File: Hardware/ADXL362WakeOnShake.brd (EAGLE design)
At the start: 43.2 x 24.1 mm, 24 parts, among them J1 PROG_HDR, U1 ADXL362, U3 ADP160-3.3

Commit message: Added attribution for original concept.
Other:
- board text added: "Original wake-on-shake concept by Nitzan Gadish, Analog Devices"
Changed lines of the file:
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@@
 <layers>
 <layer number="1" name="Top" color="4" fill="1" visible="yes" active="yes"/>
-<layer number="2" name="Route2" color="1" fill="3" visible="no" active="yes"/>
-<layer number="15" name="Route15" color="4" fill="6" visible="no" active="yes"/>
+<layer number="2" name="Route2" color="1" fill="3" visible="yes" active="yes"/>
+<layer number="15" name="Route15" color="4" fill="6" visible="yes" active="yes"/>
 <layer number="16" name="Bottom" color="1" fill="1" visible="yes" active="yes"/>
 <layer number="17" name="Pads" color="2" fill="1" visible="yes" active="yes"/>
@@
 <layer number="23" name="tOrigins" color="15" fill="1" visible="yes" active="yes"/>
 <layer number="24" name="bOrigins" color="15" fill="1" visible="yes" active="yes"/>
-<layer number="25" name="tNames" color="7" fill="1" visible="no" active="yes"/>
-<layer number="26" name="bNames" color="7" fill="1" visible="no" active="yes"/>
-<layer number="27" name="tValues" color="7" fill="1" visible="no" active="yes"/>
-<layer number="28" name="bValues" color="7" fill="1" visible="no" active="yes"/>
-<layer number="29" name="tStop" color="7" fill="3" visible="no" active="yes"/>
-<layer number="30" name="bStop" color="7" fill="6" visible="no" active="yes"/>
-<layer number="31" name="tCream" color="7" fill="4" visible="no" active="yes"/>
-<layer number="32" name="bCream" color="7" fill="5" visible="no" active="yes"/>
-<layer number="39" name="tKeepout" color="4" fill="11" visible="no" active="yes"/>
-<layer number="40" name="bKeepout" color="1" fill="11" visible="no" active="yes"/>
-<layer number="41" name="tRestrict" color="4" fill="10" visible="no" active="yes"/>
-<layer number="42" name="bRestrict" color="1" fill="10" visible="no" active="yes"/>
-<layer number="44" name="Drills" color="7" fill="1" visible="no" active="yes"/>
+<layer number="25" name="tNames" color="7" fill="1" visible="yes" active="yes"/>
+<layer number="26" name="bNames" color="7" fill="1" visible="yes" active="yes"/>
+<layer number="27" name="tValues" color="7" fill="1" visible="yes" active="yes"/>
+<layer number="28" name="bValues" color="7" fill="1" visible="yes" active="yes"/>
+<layer number="29" name="tStop" color="7" fill="3" visible="yes" active="yes"/>
+<layer number="30" name="bStop" color="7" fill="6" visible="yes" active="yes"/>
+<layer number="31" name="tCream" color="7" fill="4" visible="yes" active="yes"/>
+<layer number="32" name="bCream" color="7" fill="5" visible="yes" active="yes"/>
+<layer number="39" name="tKeepout" color="4" fill="11" visible="yes" active="yes"/>
+<layer number="40" name="bKeepout" color="1" fill="11" visible="yes" active="yes"/>
+<layer number="41" name="tRestrict" color="4" fill="10" visible="yes" active="yes"/>
+<layer number="42" name="bRestrict" color="1" fill="10" visible="yes" active="yes"/>
+<layer number="44" name="Drills" color="7" fill="1" visible="yes" active="yes"/>
 <layer number="45" name="Holes" color="7" fill="1" visible="yes" active="yes"/>
-<layer number="46" name="Milling" color="3" fill="1" visible="no" active="yes"/>
+<layer number="46" name="Milling" color="3" fill="1" visible="yes" active="yes"/>
 <layer number="51" name="tDocu" color="6" fill="1" visible="yes" active="yes"/>
-<layer number="52" name="bDocu" color="7" fill="1" visible="no" active="yes"/>
+<layer number="52" name="bDocu" color="7" fill="1" visible="yes" active="yes"/>
 <layer number="3" name="Route3" color="4" fill="3" visible="no" active="no"/>
 <layer number="4" name="Route4" color="1" fill="4" visible="no" active="no"/>
@@
 <text x="18.669" y="19.177" size="1.016" layer="21" font="vector" ratio="15">Wake-on-Shake</text>
 <text x="-46.99" y="21.59" size="1.778" layer="27" font="vector" ratio="15">M. Hord</text>
+<text x="-77.47" y="13.97" size="1.778" layer="27" font="vector" ratio="15">Original wake-on-shake concept by
+Nitzan Gadish, Analog Devices</text>
 </plain>
 <attributes>
@@
 </board>
 </drawing>
+<compatibility>
+<note version="6.3" minversion="6.2.2" severity="warning">
+Since Version 6.2.2 text objects can contain more than one line,
+which will not be processed correctly with this version.
+</note>
+</compatibility>
 </eagle>

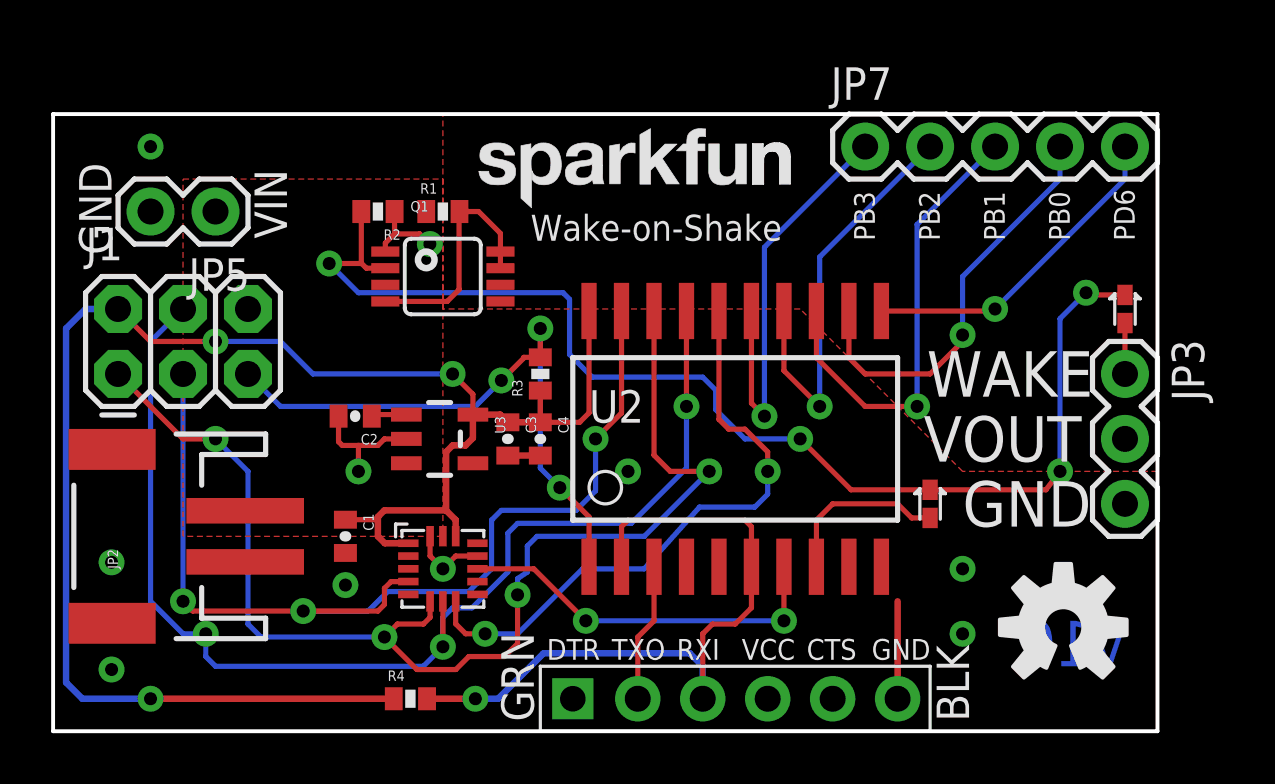
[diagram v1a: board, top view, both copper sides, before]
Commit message: Updated caps, res, sch, vers# and diodes
Updated caps/res to 0603  ,  1:1 on the adxl362, updated footprint for
diodes, new rev #
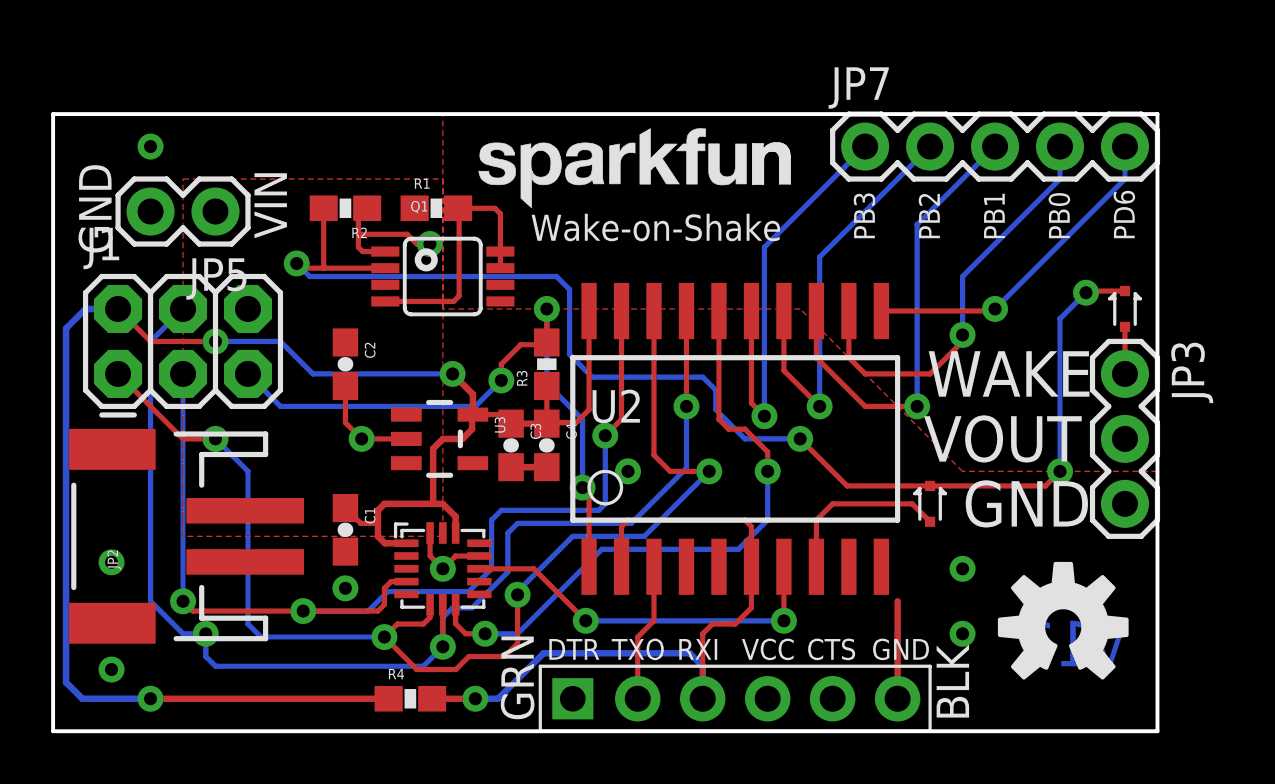
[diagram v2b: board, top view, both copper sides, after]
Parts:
- C1, C2, C3, C4: device SparkFun-Passives:0402-CAP -> SparkFun-Capacitors:0603-CAP
- R1, R2, R3, R4: device SparkFun-Passives:0402-RES -> SparkFun-Resistors:0603-RES
- U1: device SparkFun-Sensors:ADXL362 -> SparkFun-Sensors:ADXL362-1:1
- moved C2 2.07 mm to (11.4, 14.4), turned to 270 degrees
- moved R2 1.28 mm to (11.4, 20.4)
- moved R3 0.46 mm to (19.3, 14.4)
- moved C4 0.36 mm to (19.3, 11.2)
- moved C3 0.28 mm to (17.9, 11.2)
- moved R1 0.28 mm to (15.0, 20.4)
- moved C1 0.25 mm to (11.4, 7.87)
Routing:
- net N$2: track 47.6 -> 50.5 mm
- net GND: track 16.9 -> 19.0 mm
- net RESET: track 24.0 -> 25.7 mm
- net V_BATT: track 1.38 -> 0.00 mm
- net MISO: track 47.4 -> 46.5 mm
- net N$1: track 9.45 -> 10.3 mm
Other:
- board text added: "v11"
- board text removed: "v10"

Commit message: Fixed FDTI ann rings / added standoff
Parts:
- added U$4: (no value), Testing:STAND-OFF-TIGHT
- JP2: value (none) -> M02-JST-2MM-SMT
- JP5: value (none) -> M02PTH
- U$3: value OSHW-LOGOM -> (none); device SparkFun-Aesthetics:OSHW-LOGO-M -> SparkFun-Aesthetics:OSHW-LOGO-S
- moved U$3 31.2 mm to (8.41, 1.60)
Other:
- board text added: "V11"
- board text removed: "v11"
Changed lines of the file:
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@@
 <setting verticaltext="up"/>
 </settings>
-<grid distance="0.05" unitdist="inch" unit="inch" style="lines" multiple="1" display="yes" altdistance="0.005" altunitdist="inch" altunit="inch"/>
+<grid distance="0.05" unitdist="inch" unit="inch" style="lines" multiple="1" display="yes" altdistance="0.001" altunitdist="inch" altunit="inch"/>
 <layers>
 <layer number="1" name="Top" color="4" fill="1" visible="yes" active="yes"/>
@@
 <wire x1="43.18" y1="24.13" x2="0" y2="24.13" width="0.1524" layer="20"/>
 <wire x1="0" y1="24.13" x2="0" y2="0" width="0.1524" layer="20"/>
-<text x="41.91" y="2.54" size="1.778" layer="16" font="vector" ratio="15" rot="MR0">v11</text>
+<text x="13.97" y="21.59" size="1.27" layer="16" font="vector" ratio="15" rot="MR0">V11</text>
 <text x="34.163" y="13.081" size="1.778" layer="21" font="vector" ratio="15">WAKE</text>
 <text x="34.036" y="10.541" size="1.778" layer="21" font="vector" ratio="15">VOUT</text>
@@
 <text x="1.016" y="22.225" size="1.27" layer="21" font="vector" ratio="15" rot="R270">GND</text>
 <text x="7.874" y="21.971" size="1.27" layer="21" font="vector" ratio="15" rot="R270">VIN</text>
-<text x="32.131" y="19.177" size="0.8128" layer="21" font="vector" ratio="15" rot="SR90">PB3</text>
-<text x="39.751" y="19.177" size="0.8128" layer="21" font="vector" ratio="15" rot="R90">PB0</text>
-<text x="42.291" y="19.177" size="0.8128" layer="21" font="vector" ratio="15" rot="R90">PD6</text>
-<text x="37.211" y="19.177" size="0.8128" layer="21" font="vector" ratio="15" rot="R90">PB1</text>
-<text x="34.671" y="19.177" size="0.8128" layer="21" font="vector" ratio="15" rot="R90">PB2</text>
+<text x="32.385" y="18.161" size="1.27" layer="21" font="vector" ratio="15" rot="SR90">PB3</text>
+<text x="40.0812" y="18.034" size="1.27" layer="21" font="vector" ratio="15" rot="R90">PB0</text>
+<text x="42.5704" y="18.0848" size="1.27" layer="21" font="vector" ratio="15" rot="R90">PD6</text>
+<text x="37.465" y="18.1356" size="1.27" layer="21" font="vector" ratio="15" rot="R90">PB1</text>
+<text x="34.925" y="18.1102" size="1.27" layer="21" font="vector" ratio="15" rot="R90">PB2</text>
 <text x="18.669" y="19.177" size="1.016" layer="21" font="vector" ratio="15">Wake-on-Shake</text>
 <text x="-46.99" y="21.59" size="1.778" layer="27" font="vector" ratio="15">M. Hord</text>
@@
 <element name="FRAME1" library="SparkFun-Aesthetics" package="CREATIVE_COMMONS" value="FRAME-LETTER" x="-77.47" y="21.59"/>
 <element name="J1" library="SparkFun-Connectors" package="2X3" value="PROG_HDR" x="2.54" y="13.97"/>
-<element name="JP2" library="SparkFun-Connectors" package="JST-2-SMD" value="" x="3.81" y="7.62" rot="R90">
+<element name="JP2" library="SparkFun-Connectors" package="JST-2-SMD" value="M02-JST-2MM-SMT" x="3.81" y="7.62" rot="R90">
 <attribute name="PROD_ID" value="CONN-08352" x="3.81" y="7.62" size="1.778" layer="27" rot="R90" display="off"/>
 </element>
@@
 </element>
 <element name="JP4" library="SparkFun-Aesthetics" package="SFE-NEW-WEB" value="LOGO-SFENW2" x="16.637" y="20.447"/>
-<element name="U$3" library="SparkFun-Aesthetics" package="OSHW-LOGO-M" value="OSHW-LOGOM" x="39.497" y="4.064"/>
-<element name="JP5" library="SparkFun-Connectors" package="1X02" value="" x="6.35" y="20.32" rot="R180"/>
+<element name="JP5" library="SparkFun-Connectors" package="1X02" value="M02PTH" x="6.35" y="20.32" rot="R180"/>
 <element name="JP6" library="SparkFun-Aesthetics" package="SFE-NEW-WEBLOGO" value="LOGO-SFENEW" x="36.322" y="15.494" rot="MR0"/>
 <element name="JP7" library="SparkFun-Connectors" package="1X05" value="" x="31.75" y="22.86"/>
@@
 <attribute name="VALUE" value="10k" x="13.97" y="1.27" size="1.778" layer="27" display="off"/>
 </element>
+<element name="U$4" library="Testing" package="STAND-OFF-TIGHT" value="" x="39.37" y="3.81"/>
+<element name="U$3" library="SparkFun-Aesthetics" package="OSHW-LOGO-S" value="" x="8.4074" y="1.6002"/>
 </elements>
 <signals>
@@
 </signal>
 </signals>
-<errors>
-</errors>
 </board>
 </drawing>
